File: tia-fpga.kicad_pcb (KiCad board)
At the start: 2 copper layers, 72 x 100 mm, 23 parts, among them J1 PinSocket_1x24_P2.54mm_Vertic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, J2 PinHeader_1x20_P2.54mm_Vertic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, J3 PinHeader_1x20_P2.54mm_Vertic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, J4 PinSocket_1x24_P2.54mm_Vertic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, U1 SOIC-14_3.9x8.7mm_P1.27mm, U2 SOIC-20W_7.5x12.8mm_P1.27mm, U3 SOIC-20W_7.5x12.8mm_P1.27mm, U4 SOIC-20W_7.5x12.8mm_P1.27mm, U5 SOT-23-5

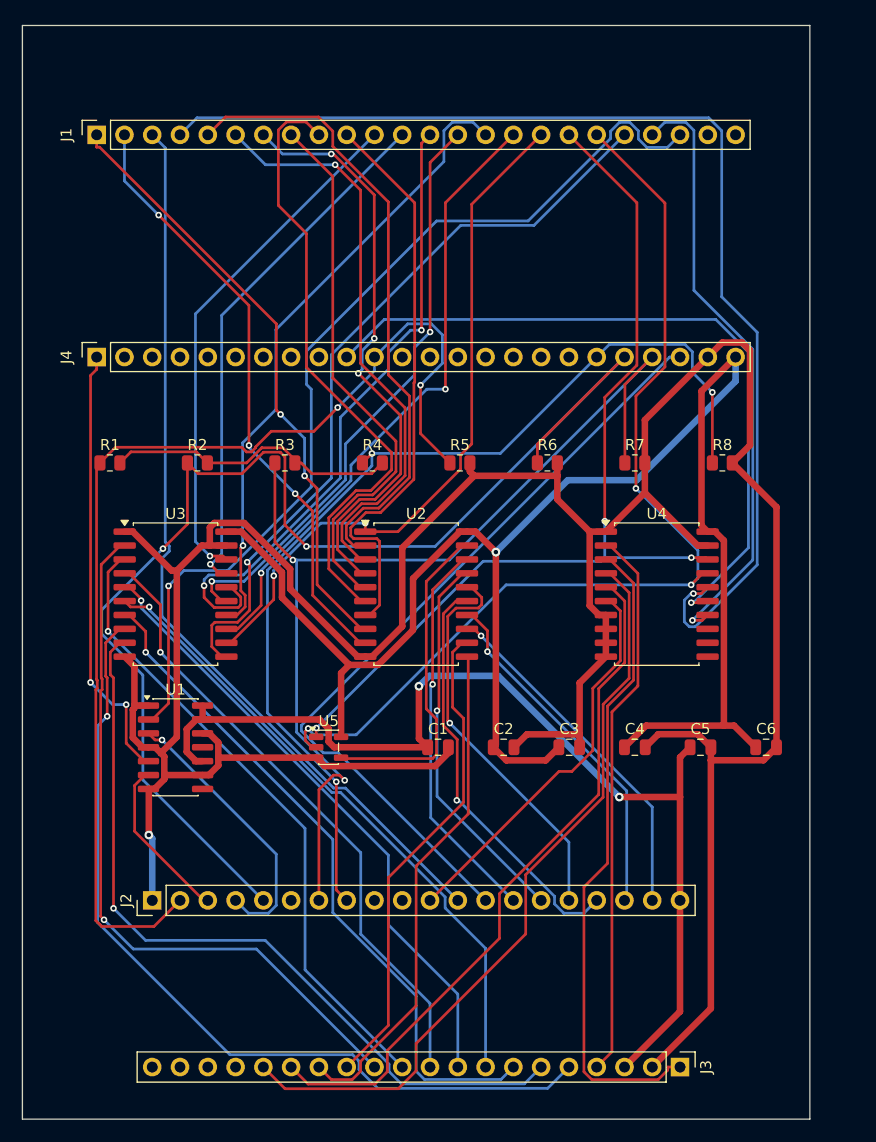
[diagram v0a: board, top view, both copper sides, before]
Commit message: Rebuild the PCB compact: the 2600 has no room for a 72 x 100 mm board
The first layout was flat — Tang Nano at one end, TIA pins at the other,
72 x 100 mm. That is wrong for the machine it plugs into. In a real 2600
the TIA, the 6507 and the RIOT sit millimetres apart, ringed by resistor
networks and the cartridge slot; that board would have fouled half the
console.

Rebuilt as a stack. All four connector rows are now concentric on the
2.54 mm grid — Tang Nano rows at y 5.84 and 26.16 (20.32 mm apart), TIA
rows at 8.38 and 23.62 (15.24 mm, fixed by the package) — so the two
pitches interleave and the board shrinks to 70 x 32 mm, roughly the Tang
Nano's own footprint. That is 29% of the previous area.

Logic goes in the 15.24 mm channel between the DIP rows. The SOIC-20W
lead span is 10.30 mm against 13.54 mm of clear channel, so the packages
the user chose still fit and no repackaging was needed; passives moved to
the outer margins.

Routing needed a perturbation pass. The first run stalled at two
connections (/F_A5, /TIA_CS3_N) with the score oscillating over 19
passes: the channel leaves 1.10 mm between header pads and SOIC pads, and
at 0.20 mm clearance one track eats 0.55 mm of it. Dropping clearance to
0.15 mm routed all 109 connections in 17.9 s. 738 segments, 49 vias,
2.04 m of copper — down from 3.72 m.

Note for anyone rerunning this: pcbnew rewrites the .kicad_pro on
SaveBoard, so the netclass clearance has to be written back AFTER the
last save or DRC checks the routed board against the wrong rule. That
cost 346 phantom clearance violations before it was spotted.

DRC: 0 clearance, 0 unconnected, 0 shorts. Nine courtyard overlaps
remain and are verified false positives — KiCad's SOIC courtyard is
11.95 mm tall against 11.61 mm of channel, but the parts clear each other
by 1.10 mm in copper and 2.60 mm body to body. Six cosmetic silkscreen
violations are documented rather than papered over.

The README now also flags that the board overhangs the neighbouri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
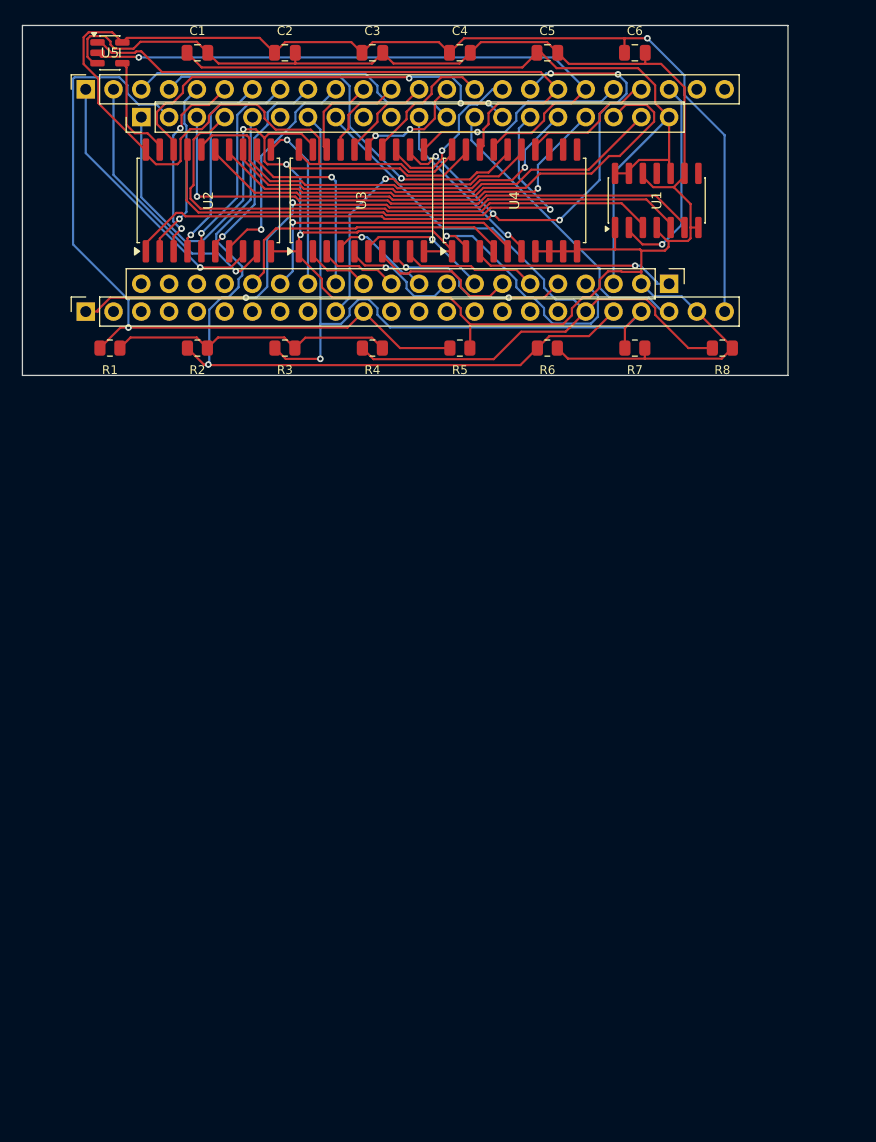
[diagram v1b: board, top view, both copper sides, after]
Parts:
- moved J2 71.6 mm to (10.9, 8.38)
- moved J3 71.6 mm to (59.1, 23.6)
- moved C1 67.2 mm to (16.0, 2.50)
- moved U1 66.6 mm to (58.0, 16.0), turned to 90 degrees
- moved C2 66.6 mm to (24.0, 2.50)
- moved U5 66.6 mm to (8.00, 2.50)
- moved C3 66.0 mm to (32.0, 2.50)
- moved C4 65.5 mm to (40.0, 2.50)
- moved C5 65.0 mm to (48.0, 2.50)
- moved C6 64.6 mm to (56.0, 2.50)
- moved U2 40.7 mm to (17.0, 16.0), turned to 90 degrees
- moved U3 39.8 mm to (31.0, 16.0), turned to 90 degrees
- moved U4 38.3 mm to (45.0, 16.0), turned to 90 degrees
- moved R1 10.5 mm to (8.00, 29.5)
- moved R2 10.5 mm to (16.0, 29.5)
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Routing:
- net /F_PHI0: track 87.6 -> 19.2 mm
- net /F_I4: track 105.5 -> 38.8 mm
- net /TIA_RW: track 78.9 -> 17.8 mm, vias 1 -> 2
- net /TIA_A0: track 65.9 -> 6.10 mm, vias 1 -> 0
- net /TIA_PHI2: track 72.0 -> 12.4 mm, vias 1 -> 0
- net /F_AU1: track 82.8 -> 30.6 mm
- net /TIA_A1: track 58.4 -> 7.34 mm, vias 1 -> 0
- net /F_A2: track 59.5 -> 8.88 mm, vias 2 -> 0
- net /F_LUM1: track 117.9 -> 68.3 mm, vias 2 -> 1
- net /F_PHI2: track 69.5 -> 20.0 mm
- net /TIA_A5: track 62.7 -> 13.9 mm, vias 1 -> 0
- net /TIA_A2: track 56.9 -> 9.69 mm
- net /TIA_A3: track 56.7 -> 11.2 mm
- net /TIA_A4: track 57.7 -> 12.3 mm
- net /F_A4: track 58.1 -> 12.8 mm, vias 1 -> 0
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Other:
- board size 72 x 100 mm -> 70 x 32 mm

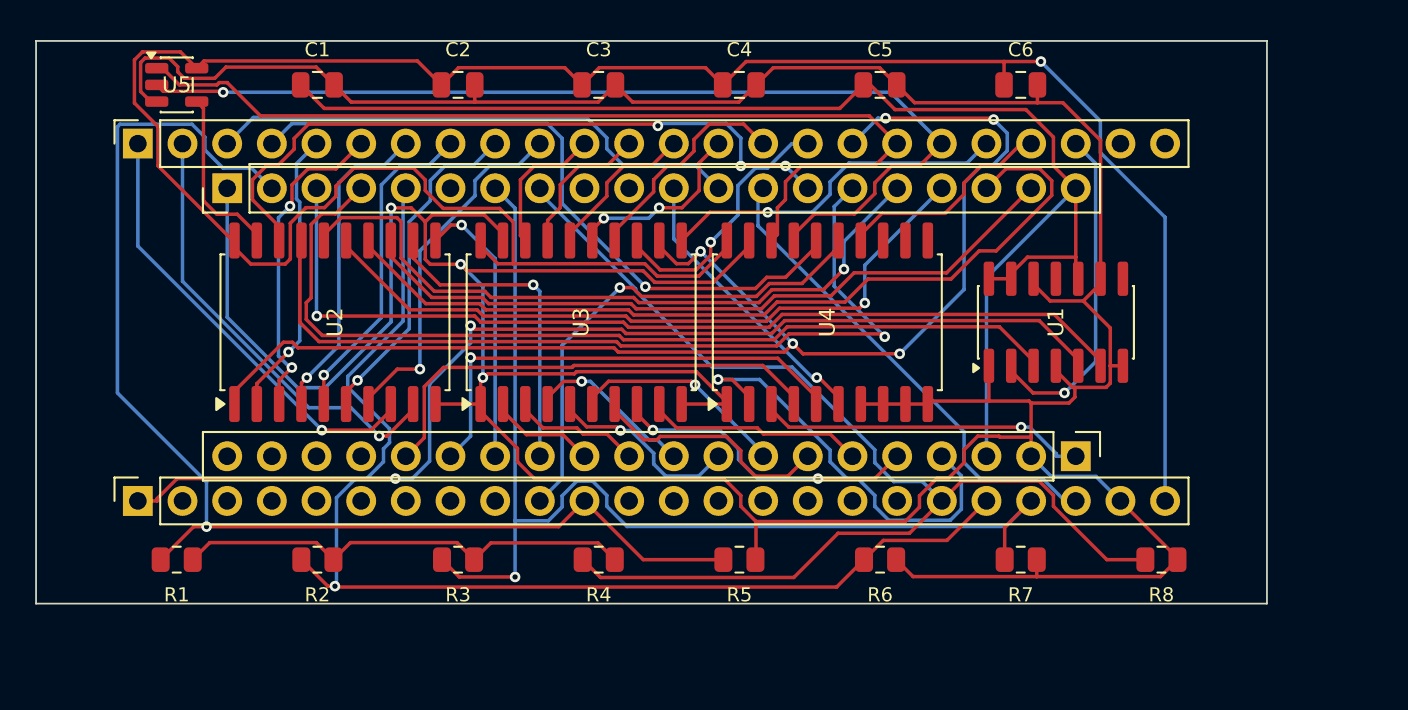
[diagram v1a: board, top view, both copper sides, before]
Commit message: Put the TIA pins on the back, add mounting holes and a ground pour, fit chroma
Four changes, one of them a real bug.

THE BUG: all four connectors were on the front. The Tang Nano sockets and
the TIA pin headers were mounted on the same side, which means the board
could never have gone into a socket — the pins pointed up alongside the
sockets instead of down. J2/J3 now sit on B.Cu. Flipping mirrors the pad
order, so the placement loop checks which end pin 1 landed on and spins
the part 180 degrees about its own pad centre when it is wrong; J2 keeps
pin 1 at the left, J3 at the right, preserving the DIP-40 wrap-around.

This also removed the nine courtyard overlaps for free: with the headers
on the back and the SMD logic on the front, they no longer share space,
so KiCad's generous SOIC courtyard has nothing to collide with.

CHROMA IS BACK. F_COL took the pin that carried PHI2. The trade is sound:
the FPGA generates PHI0 itself, so it knows where it is in the bus cycle
and can time accesses from its own clock rather than the 6507's output.
It costs a little timing fidelity and buys back colour on the composite
and RF path. That matters because the likeliest use of this board is not
a bench rig — it is reviving a console with a dead TIA while keeping its
original video. R9 comes back with it, and the README now spells out that
R1-R9 must be left unpopulated in a real 2600, where the console already
has that ladder and a second one in parallel would shift every level.
PHI2 is still buffered by U3 and brought to an unconnected pad.

MOUNTING HOLES: four M2 in the corners. The board grew to 76 x 36 mm to
make room for them without crowding the connector rows.

GROUND POUR: 1418 mm2 on B.Cu, filled after routing. It has to be after —
Freerouting reads a pour as an obstacle and goes effectively single-layer
with one present.

Routing needed one more perturbation than before: 0.15 mm clearance left
F_I5 unrouted, 0.13 mm routed all 111 connections in 22.6 s. 758
segments, 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
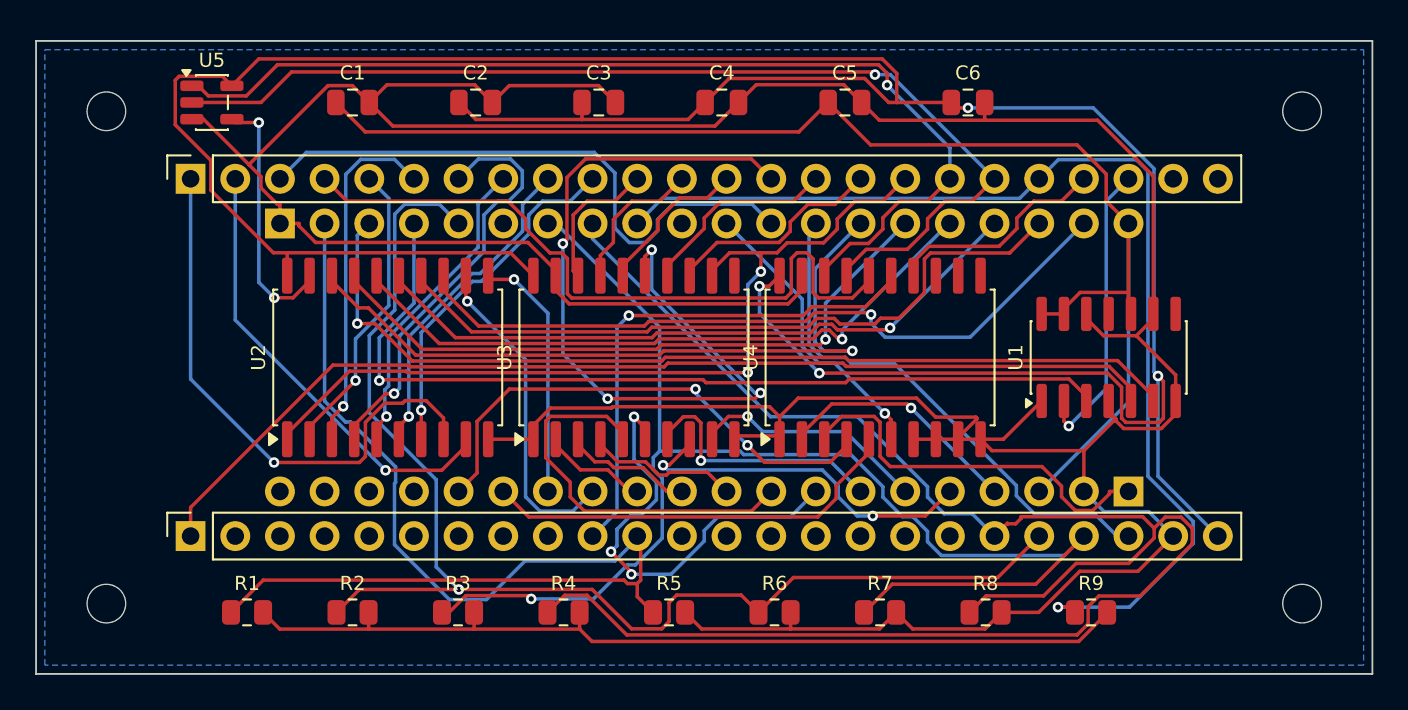
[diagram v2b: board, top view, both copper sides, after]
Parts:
- added H1: MountingHole_2.2mm_M2, MountingHole_2.2mm_M2, F.Cu at (4.00, 4.00)
- added H2: MountingHole_2.2mm_M2, MountingHole_2.2mm_M2, F.Cu at (72.0, 4.00)
- added H3: MountingHole_2.2mm_M2, MountingHole_2.2mm_M2, F.Cu at (4.00, 32.0)
- added H4: MountingHole_2.2mm_M2, MountingHole_2.2mm_M2, F.Cu at (72.0, 32.0)
- added R9: R_0805_2012Metric, R_0805_2012Metric, F.Cu at (60.0, 32.5)
- J2, J3: moved to B.Cu
- moved R8 10.4 mm to (54.0, 32.5)
- moved R7 8.54 mm to (48.0, 32.5)
- moved R6 6.71 mm to (42.0, 32.5)
- moved R1 5.00 mm to (12.0, 32.5)
- moved R5 5.00 mm to (36.0, 32.5)
- moved J2 3.61 mm to (13.9, 10.4), turned to -90 degrees
- moved J3 3.61 mm to (62.1, 25.6), turned to 90 degrees
- moved R2 3.61 mm to (18.0, 32.5)
- moved R4 3.61 mm to (30.0, 32.5)
- moved U1 3.61 mm to (61.0, 18.0)
- moved U2 3.61 mm to (20.0, 18.0)
- moved U3 3.61 mm to (34.0, 18.0)
- moved U4 3.61 mm to (48.0, 18.0)
- moved J1 3.61 mm to (8.79, 7.84)
- moved J4 3.61 mm to (8.79, 28.2)
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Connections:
- J1 pad 20: /F_PHI2 -> /F_COL
- J2 pad 9: unconnected-(J2-Pin_9-Pad9) -> /F_COL
- U3 pad 11: /F_PHI2 -> unconnected-(U3-Y7-Pad11)
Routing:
- net /F_COL: track 0.00 -> 63.3 mm, vias 0 -> 1
- net /F_A3: track 10.7 -> 47.6 mm, vias 2 -> 4
- net +3V3: track 137.5 -> 171.3 mm, vias 1 -> 4
- net /F_LUM0: track 67.8 -> 98.1 mm
- net /F_RW: track 76.4 -> 48.9 mm, vias 5 -> 2
- net GND: track 259.1 -> 232.7 mm, vias 3 -> 0
- net /VIDEO_SUM: track 26.4 -> 52.2 mm
- net /F_PHI2: track 20.0 -> 0.00 mm, vias 1 -> 0
- net /F_LUM2: track 63.8 -> 77.6 mm
- net /TIA_A4: track 12.3 -> 25.7 mm, vias 1 -> 3
- net /TIA_D1: track 48.9 -> 37.4 mm
- net /TIA_A3: track 11.2 -> 22.4 mm, vias 1 -> 0
- net /TIA_CS0_N: track 24.2 -> 14.0 mm
- net /TIA_D4: track 48.9 -> 40.6 mm
- net /F_D6: track 25.4 -> 31.9 mm
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- added copper zone on B.Cu, net GND
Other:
- board size 70 x 32 mm -> 76 x 36 mm
